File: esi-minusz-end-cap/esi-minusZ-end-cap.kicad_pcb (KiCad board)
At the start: 4 copper layers, 105.6 x 105.6 mm, 46 parts, among them J1 M55-7011242R, J2 U.FL-R-SMA, U1 RM3100, U2 RM3100

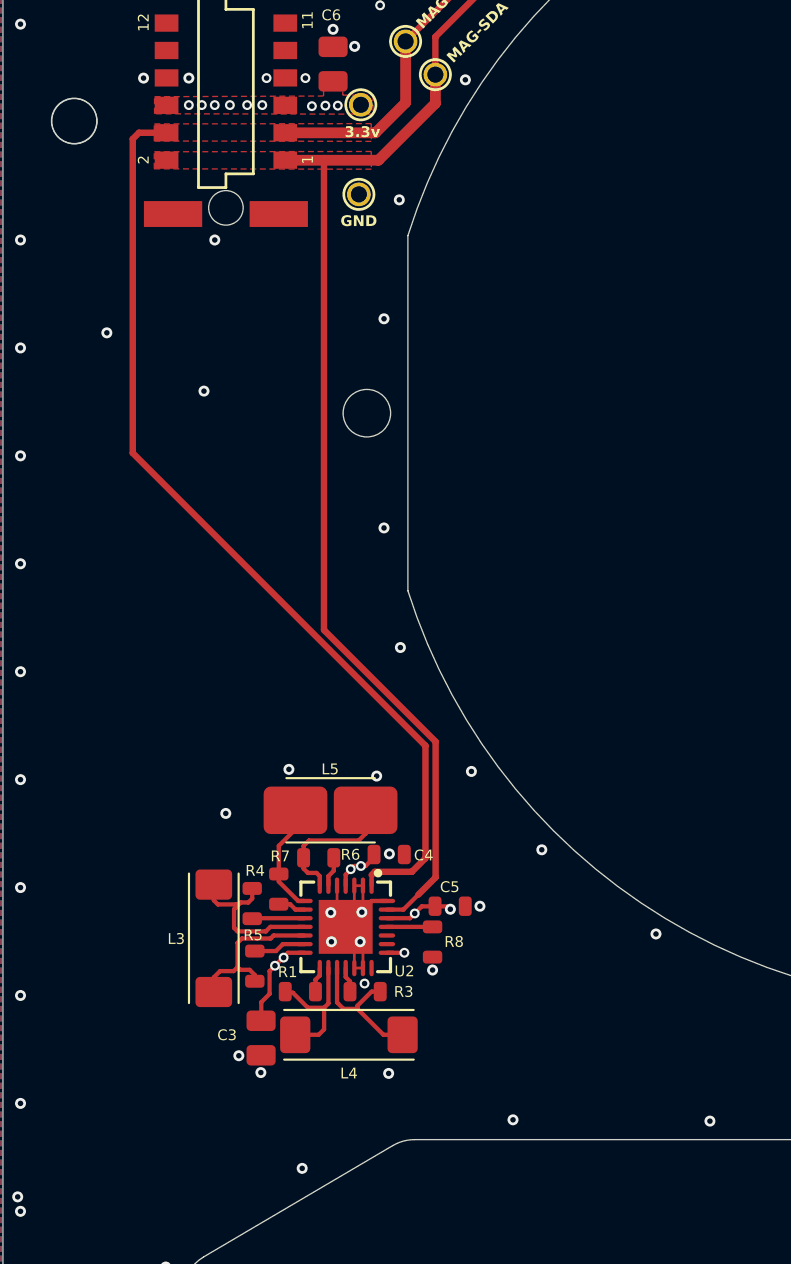
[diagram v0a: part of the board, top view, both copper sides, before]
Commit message: New ESI dxf w/ square cutout
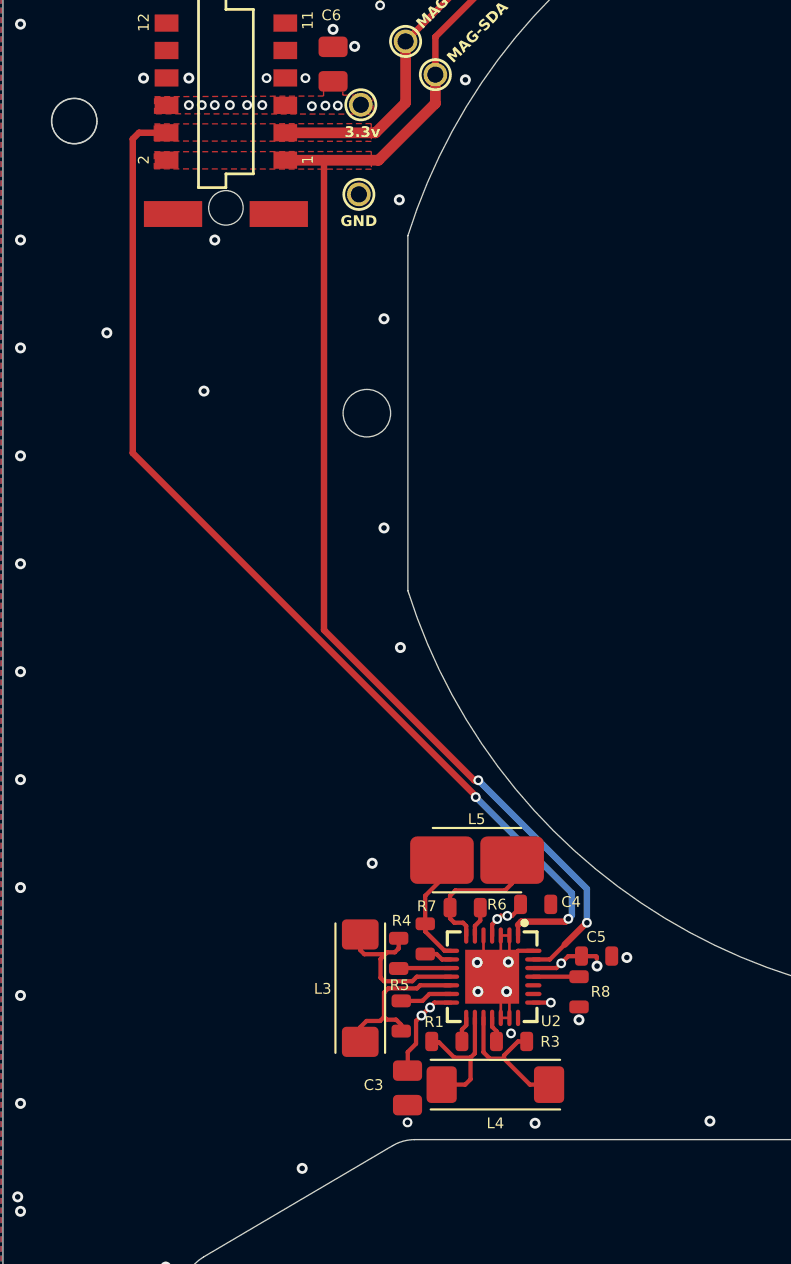
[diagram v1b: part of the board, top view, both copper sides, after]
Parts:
- moved C3 7.17 mm to (114.4, 122.3)
- moved L5 7.17 mm to (117.7, 111.7)
- moved C4 7.17 mm to (120.4, 113.8)
- moved C5 7.17 mm to (123.2, 116.2)
- moved L3 7.17 mm to (112.2, 117.7)
- moved R4 7.17 mm to (114.0, 116.0)
- moved R5 7.17 mm to (114.1, 119.0)
- moved R6 7.17 mm to (117.1, 113.9)
- moved R8 7.17 mm to (122.4, 117.8)
- moved U2 7.17 mm to (118.3, 117.1)
- moved L4 7.17 mm to (118.5, 122.1)
- moved R1 7.17 mm to (116.2, 120.1)
- moved R3 7.17 mm to (119.2, 120.1)
- moved R7 7.17 mm to (115.2, 115.4)
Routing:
- net /MAG-SDA: track 141.6 -> 147.1 mm, vias 0 -> 2
- net /MAG-SCL: track 133.4 -> 138.7 mm, vias 0 -> 2
- net GND: vias 203 -> 195

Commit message: Update -Z endcap DFX
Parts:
- moved C4 4.32 mm to (124.4, 112.1)
- moved C5 4.32 mm to (127.2, 114.5)
- moved L3 4.32 mm to (116.2, 116.0)
- moved R4 4.32 mm to (118.0, 114.4)
- moved R6 4.32 mm to (121.1, 112.3)
- moved U2 4.32 mm to (122.3, 115.5)
- moved C3 4.32 mm to (118.4, 120.6)
- moved L4 4.32 mm to (122.5, 120.5)
- moved L5 4.32 mm to (121.6, 110.1)
- moved R1 4.32 mm to (120.2, 118.5)
- moved R3 4.32 mm to (123.2, 118.5)
- moved R5 4.32 mm to (118.1, 117.3)
- moved R7 4.32 mm to (119.2, 113.7)
- moved R8 4.32 mm to (126.4, 116.2)
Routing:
- net /MAG-SCL: track 138.7 -> 136.2 mm, vias 2 -> 0
- net /MAG-SDA: track 147.1 -> 144.8 mm, vias 2 -> 0
- net GND: vias 195 -> 193
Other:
- outline, holes or cut-outs redrawn
